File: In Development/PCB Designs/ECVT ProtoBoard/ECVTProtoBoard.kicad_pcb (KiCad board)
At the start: 2 copper layers, 26 parts, among them J1 Motor Driver, J10 3V3, J11 GND, J12 Hall Effect, J13 Hall Effect 2, J14 12V In, J15 Conn_01x08, J16 MotorDriver2, J17 GND In, J2 Conn_01x01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

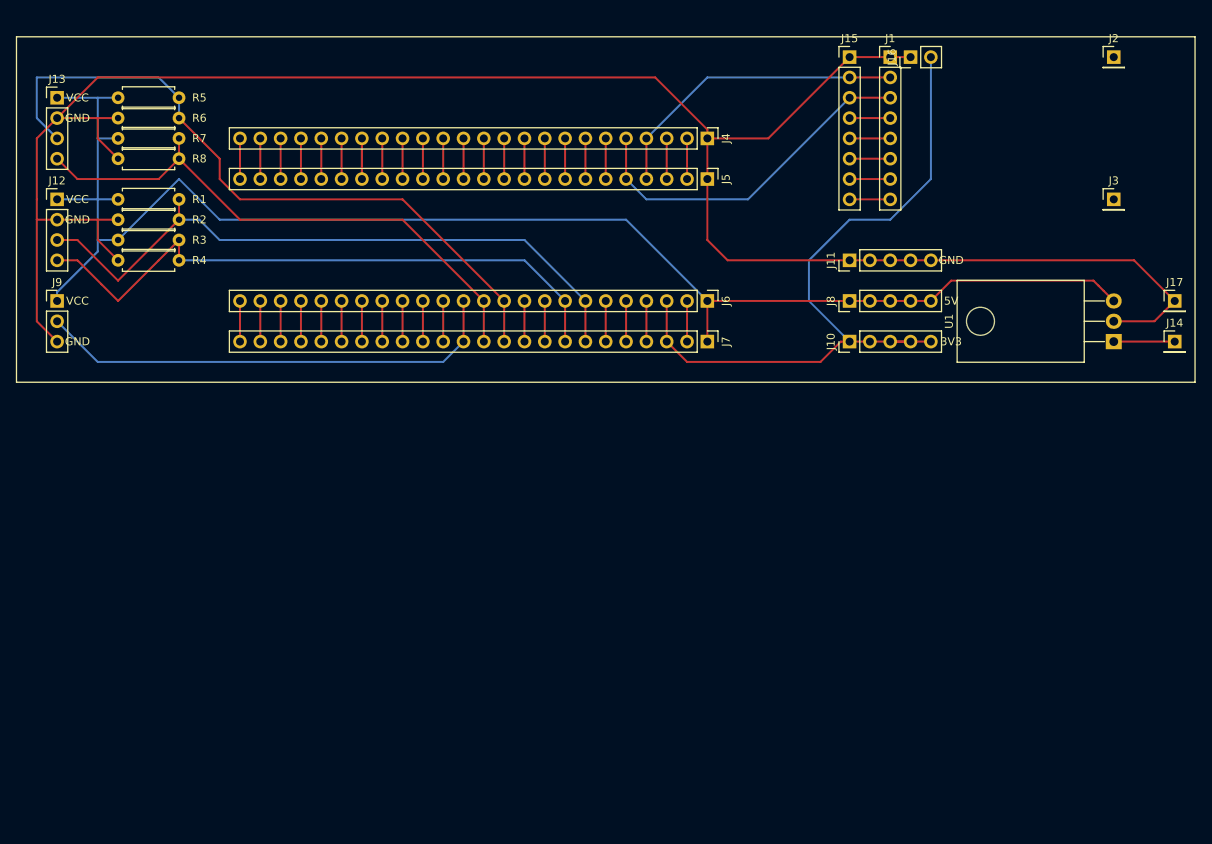
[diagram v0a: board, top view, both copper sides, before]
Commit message: Finished eCVT protoboard schematic
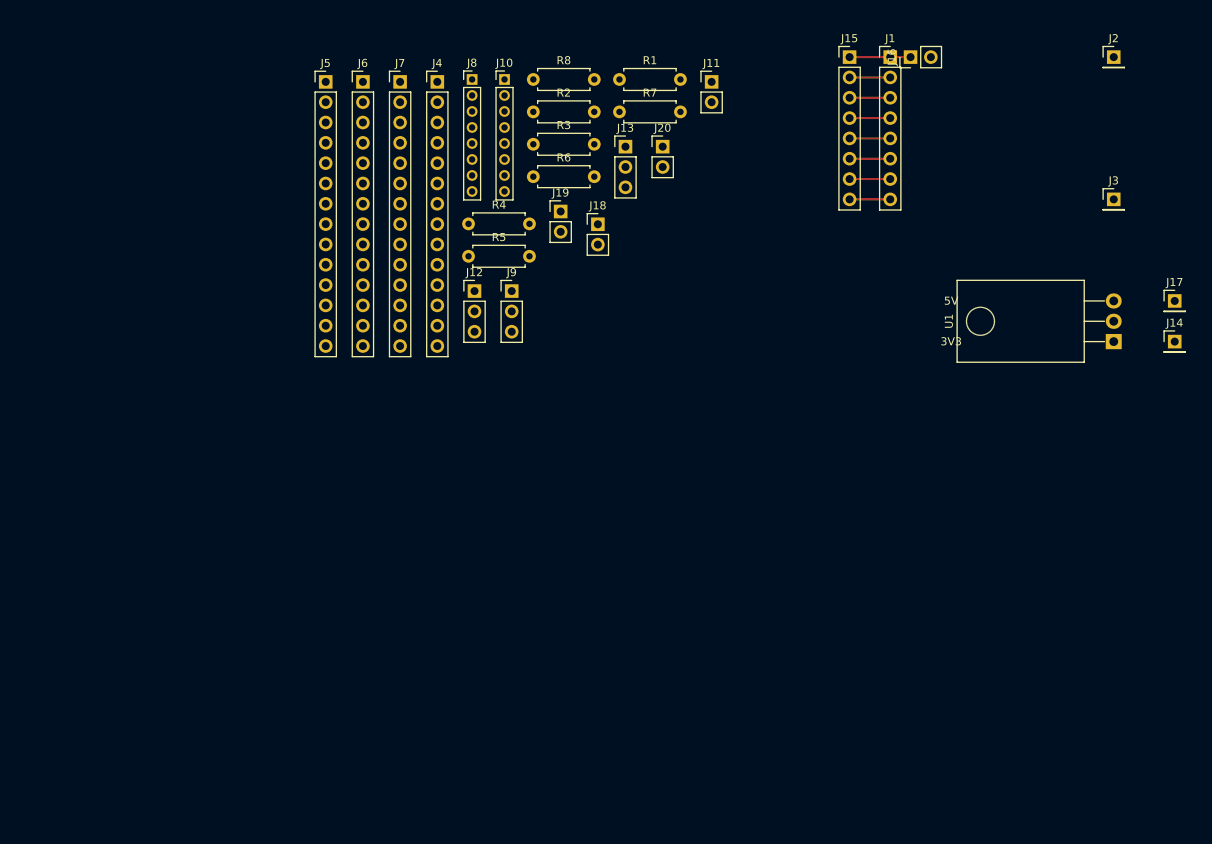
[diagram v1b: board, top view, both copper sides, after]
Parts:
- added J18: 3V3, Connector_PinHeader_2.54mm:PinHeader_1x02_P2.54mm_Vertical, F.Cu at (133.6, 92.0)
- added J19: GND, Connector_PinHeader_2.54mm:PinHeader_1x02_P2.54mm_Vertical, F.Cu at (129.0, 90.4)
- added J20: BrakeIn, Connector_PinHeader_2.54mm:PinHeader_1x02_P2.54mm_Vertical, F.Cu at (141.7, 82.3)
- J10: value 3V3 -> Conn_01x08; footprint Connector_PinHeader_2.54mm:PinHeader_1x05_P2.54mm_Vertical -> Connector_PinHeader_2.00mm:PinHeader_1x08_P2.00mm_Vertical
- J11: value GND -> 5V; footprint Connector_PinHeader_2.54mm:PinHeader_1x05_P2.54mm_Vertical -> Connector_PinHeader_2.54mm:PinHeader_1x02_P2.54mm_Vertical
- J12: footprint Connector_PinHeader_2.54mm:PinHeader_1x04_P2.54mm_Vertical -> Connector_PinHeader_2.54mm:PinHeader_1x03_P2.54mm_Vertical
- J13: value Hall Effect 2 -> Hall Effect; footprint Connector_PinHeader_2.54mm:PinHeader_1x04_P2.54mm_Vertical -> Connector_PinHeader_2.54mm:PinHeader_1x03_P2.54mm_Vertical
- J4, J7: value 1x24 -> 1x14; footprint Connector_PinHeader_2.54mm:PinHeader_1x24_P2.54mm_Vertical -> Connector_PinHeader_2.54mm:PinHeader_1x14_P2.54mm_Vertical
- J5: value Teensy 3.6L -> Teensy 3.2L; footprint Connector_PinHeader_2.54mm:PinHeader_1x24_P2.54mm_Vertical -> Connector_PinHeader_2.54mm:PinHeader_1x14_P2.54mm_Vertical
- J6: value Teensy 3.6R -> Teensy 3.2R; footprint Connector_PinHeader_2.54mm:PinHeader_1x24_P2.54mm_Vertical -> Connector_PinHeader_2.54mm:PinHeader_1x14_P2.54mm_Vertical
- J8: value 5V -> Conn_01x08; footprint Connector_PinHeader_2.54mm:PinHeader_1x05_P2.54mm_Vertical -> Connector_PinHeader_2.00mm:PinHeader_1x08_P2.00mm_Vertical
- R3, R7: value 5.1k -> 4.7k
- moved J13 71.3 mm to (137.1, 82.3)
- moved R1 57.1 mm to (136.3, 73.9), turned to 0 degrees
- moved J9 56.8 mm to (122.9, 100.4)
- moved R7 55.2 mm to (136.3, 78.0), turned to 0 degrees
- moved J8 54.7 mm to (117.9, 73.9), turned to 0 degrees
- moved J10 54.2 mm to (122.0, 73.9), turned to 0 degrees
- moved J12 53.4 mm to (118.2, 100.4)
- moved J6 51.0 mm to (104.3, 74.2), turned to 0 degrees
- moved J7 50.3 mm to (108.9, 74.2), turned to 0 degrees
- moved J5 49.2 mm to (99.6, 74.2), turned to 0 degrees
- moved R2 46.3 mm to (125.6, 78.0), turned to 0 degrees
- moved R3 45.9 mm to (125.6, 82.0), turned to 0 degrees
- moved R8 45.4 mm to (125.6, 73.9), turned to 0 degrees
- moved R6 44.9 mm to (125.6, 86.1), turned to 0 degrees
- moved R5 41.3 mm to (117.5, 96.0), turned to 0 degrees
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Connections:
- J10 pad 2: Net-(J10-Pad1) -> (no net)
- J10 pad 3: Net-(J10-Pad1) -> Net-(J1-Pad1)
- J10 pad 4: Net-(J10-Pad1) -> Net-(J10-Pad4)
- J10 pad 5: Net-(J10-Pad1) -> (no net)
- J11 pad 1: Net-(J1-Pad1) -> Net-(J10-Pad1)
- J11 pad 2: Net-(J1-Pad1) -> Net-(J10-Pad1)
- J12 pad 1: Net-(J12-Pad1) -> Net-(J10-Pad1)
- J12 pad 3: Net-(J12-Pad3) -> Net-(J10-Pad8)
- J13 pad 1: Net-(J12-Pad1) -> Net-(J10-Pad1)
- J13 pad 3: Net-(J13-Pad3) -> Net-(J10-Pad4)
- J16 pad 2: Net-(J10-Pad1) -> Net-(J16-Pad2)
- J4 pad 7: Net-(J4-Pad7) -> Net-(J10-Pad8)
- J4 pad 8: Net-(J4-Pad8) -> Net-(J10-Pad4)
- J5 pad 7: Net-(J4-Pad7) -> Net-(J10-Pad8)
- J5 pad 8: Net-(J4-Pad8) -> Net-(J10-Pad4)
- J6 pad 1: Net-(J12-Pad1) -> Net-(J10-Pad1)
- J6 pad 11: Net-(J13-Pad3) -> Net-(J6-Pad11)
- J6 pad 12: Net-(J13-Pad4) -> Net-(J6-Pad12)
- J6 pad 3: Net-(J10-Pad1) -> Net-(J16-Pad2)
- J6 pad 7: Net-(J12-Pad3) -> Net-(J6-Pad7)
- J6 pad 8: Net-(J12-Pad4) -> Net-(J6-Pad8)
- J7 pad 1: Net-(J12-Pad1) -> Net-(J10-Pad1)
- J7 pad 11: Net-(J13-Pad3) -> Net-(J6-Pad11)
- J7 pad 12: Net-(J13-Pad4) -> Net-(J6-Pad12)
- J7 pad 3: Net-(J10-Pad1) -> Net-(J16-Pad2)
- J7 pad 7: Net-(J12-Pad3) -> Net-(J6-Pad7)
- J7 pad 8: Net-(J12-Pad4) -> Net-(J6-Pad8)
- J8 pad 1: Net-(J12-Pad1) -> (no net)
- J8 pad 2: Net-(J12-Pad1) -> (no net)
- J8 pad 3: Net-(J12-Pad1) -> (no net)
- J8 pad 4: Net-(J12-Pad1) -> (no net)
- J8 pad 5: Net-(J12-Pad1) -> (no net)
- J9 pad 1: Net-(J12-Pad1) -> Net-(J16-Pad2)
- R1 pad 1: Net-(J12-Pad3) -> Net-(J10-Pad8)
- R1 pad 2: Net-(J12-Pad1) -> Net-(J10-Pad1)
- R2 pad 1: Net-(J12-Pad3) -> Net-(J10-Pad8)
- R3 pad 1: Net-(J12-Pad4) -> Net-(J6-Pad12)
- R3 pad 2: Net-(J12-Pad1) -> Net-(J20-Pad1)
- R4 pad 1: Net-(J12-Pad4) -> Net-(J1-Pad1)
- R4 pad 2: Net-(J1-Pad1) -> Net-(J6-Pad12)
- R5 pad 1: Net-(J13-Pad3) -> Net-(J10-Pad4)
- R5 pad 2: Net-(J12-Pad1) -> Net-(J10-Pad1)
- R6 pad 1: Net-(J13-Pad3) -> Net-(J10-Pad4)
- R7 pad 1: Net-(J13-Pad4) -> Net-(J6-Pad11)
- R7 pad 2: Net-(J12-Pad1) -> Net-(J20-Pad2)
- R8 pad 1: Net-(J13-Pad4) -> Net-(J1-Pad1)
- R8 pad 2: Net-(J1-Pad1) -> Net-(J6-Pad11)
- U1 pad 3: Net-(J12-Pad1) -> Net-(J10-Pad1)
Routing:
- net Net-(J1-Pad1): track 259.8 -> 7.62 mm
- net Net-(J12-Pad1): track 188.9 -> 0.00 mm
- net Net-(J10-Pad1): track 89.7 -> 0.00 mm
- net Net-(J13-Pad3): track 86.7 -> 0.00 mm
- net Net-(J12-Pad3): track 83.1 -> 0.00 mm
- net Net-(J12-Pad4): track 78.5 -> 0.00 mm
- net Net-(J13-Pad4): track 70.4 -> 0.00 mm
- net Net-(J6-Pad13): track 59.0 -> 0.00 mm
- net Net-(J1-Pad3): track 44.4 -> 5.08 mm
- net Net-(J1-Pad2): track 38.7 -> 5.08 mm
- net Net-(J4-Pad18): track 9.36 -> 0.00 mm
- net Net-(J14-Pad1): track 7.62 -> 0.00 mm
- net Net-(J6-Pad9): track 5.08 -> 0.00 mm
- net Net-(J6-Pad6): track 5.08 -> 0.00 mm
- net Net-(J6-Pad5): track 5.08 -> 0.00 mm
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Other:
- board text removed: "GND"
- board text removed: "VCC"

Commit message: Routed the board
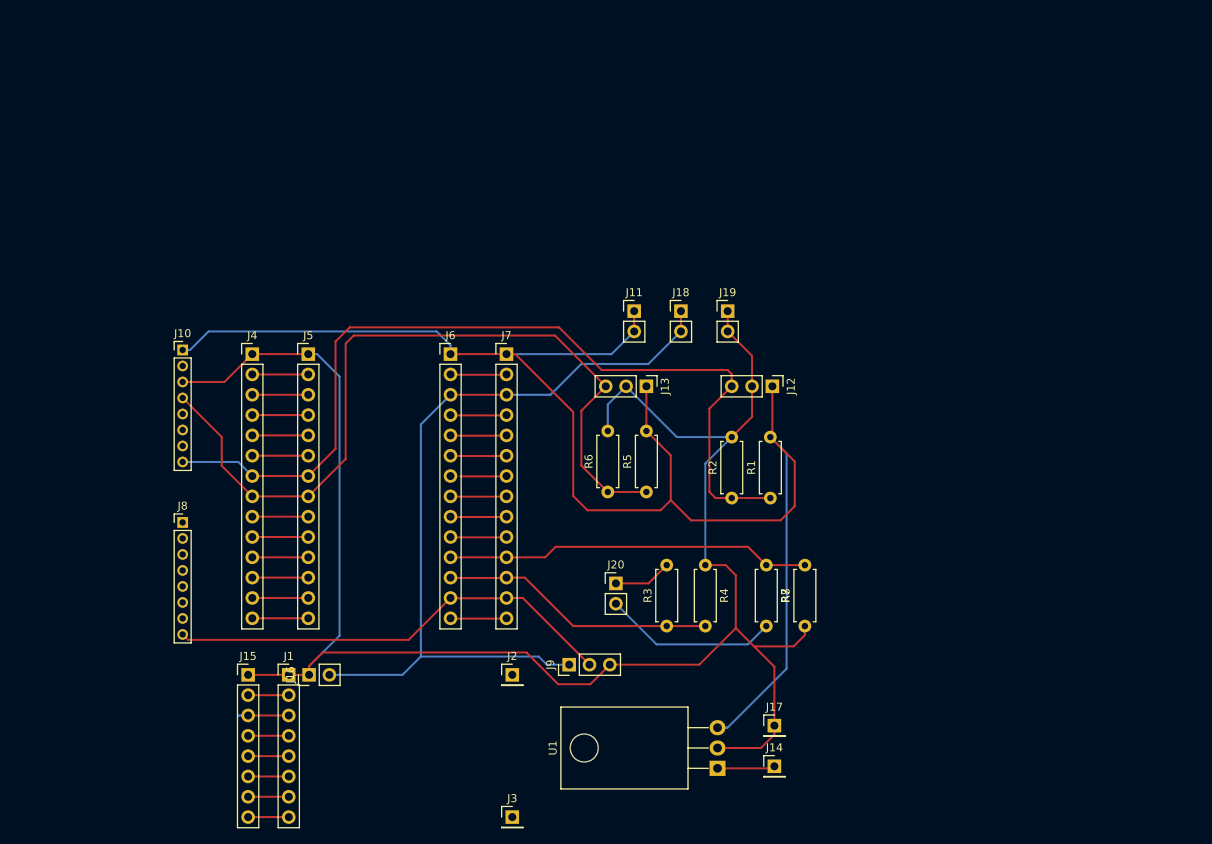
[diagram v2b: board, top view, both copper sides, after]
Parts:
- moved J1 107.8 mm to (95.0, 148.3)
- moved J15 107.8 mm to (89.9, 148.3)
- moved J16 107.8 mm to (97.5, 148.3)
- moved J2 107.8 mm to (122.9, 148.3)
- moved J3 107.8 mm to (122.9, 166.1)
- moved R8 76.3 mm to (159.5, 142.2), turned to 90 degrees
- moved J17 73.0 mm to (155.7, 154.7)
- moved J14 73.0 mm to (155.7, 159.8)
- moved U1 72.8 mm to (148.6, 160.0)
- moved J8 66.1 mm to (81.7, 129.3)
- moved R3 62.5 mm to (142.2, 142.2), turned to 90 degrees
- moved R7 59.6 mm to (154.7, 134.6), turned to 270 degrees
- moved R1 55.6 mm to (155.2, 126.2), turned to 90 degrees
- moved J20 54.9 mm to (135.9, 136.9)
- moved R2 54.3 mm to (150.4, 126.2), turned to 90 degrees
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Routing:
- net Net-(J1-Pad1): track 7.62 -> 228.3 mm
- net Net-(J10-Pad1): track 0.00 -> 188.8 mm
- net Net-(J10-Pad8): track 0.00 -> 111.2 mm
- net Net-(J16-Pad2): track 0.00 -> 100.2 mm
- net Net-(J10-Pad4): track 0.00 -> 100.2 mm
- net Net-(J6-Pad13): track 0.00 -> 56.8 mm
- net Net-(J6-Pad11): track 0.00 -> 45.8 mm
- net Net-(J6-Pad12): track 0.00 -> 34.4 mm
- net Net-(J20-Pad2): track 0.00 -> 21.8 mm
- net Net-(J1-Pad3): track 5.08 -> 13.4 mm
- net Net-(J20-Pad1): track 0.00 -> 7.30 mm
- net Net-(J14-Pad1): track 0.00 -> 7.22 mm
- net Net-(J6-Pad9): track 0.00 -> 7.00 mm
- net Net-(J6-Pad8): track 0.00 -> 7.00 mm
- net Net-(J6-Pad6): track 0.00 -> 7.00 mm
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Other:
- board text removed: "3V3"
- board text removed: "5V"

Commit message: Finished eCVT PCB rev 2
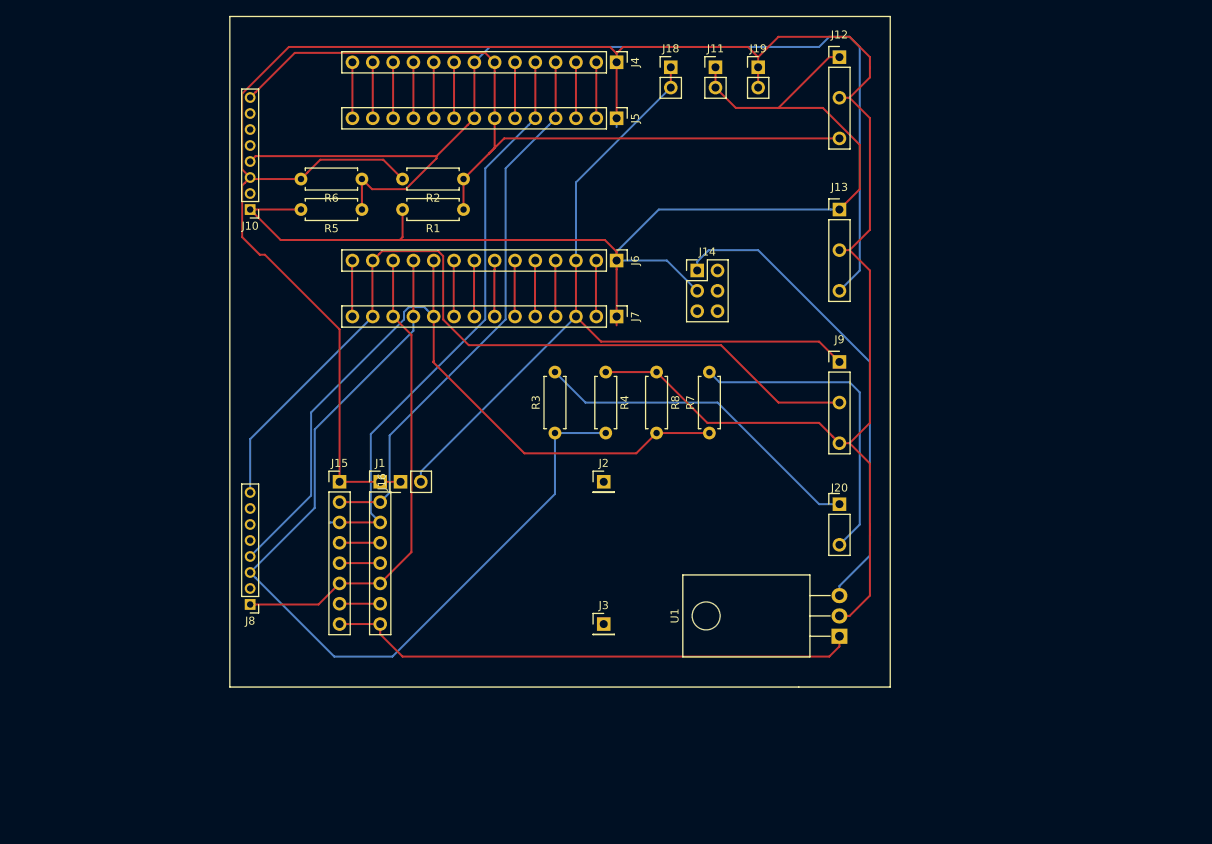
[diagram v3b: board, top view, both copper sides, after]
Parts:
- removed J17: GND In, Connector_PinHeader_2.54mm:PinHeader_1x01_P2.54mm_Vertical
- J12, J13, J9: footprint Connector_PinHeader_2.54mm:PinHeader_1x03_P2.54mm_Vertical -> CustomKiCADLibrary:PinHeader_1x03_P5.08mm_Vertical
- J14: value 12V In -> External Power Switch; footprint Connector_PinHeader_2.54mm:PinHeader_1x01_P2.54mm_Vertical -> Connector_PinHeader_2.54mm:PinHeader_2x03_P2.54mm_Vertical
- J20: footprint Connector_PinHeader_2.54mm:PinHeader_1x02_P2.54mm_Vertical -> CustomKiCADLibrary:PinHeader_1x02_P5.08mm_Vertical
- moved J14 62.7 mm to (146.1, 97.8)
- moved J4 58.3 mm to (136.0, 71.8), turned to 270 degrees
- moved R1 52.6 mm to (116.8, 90.2), turned to 180 degrees
- moved R2 52.1 mm to (116.8, 86.4), turned to 180 degrees
- moved J9 50.7 mm to (163.8, 109.2), turned to 0 degrees
- moved R5 50.1 mm to (104.1, 90.2), turned to 180 degrees
- moved R6 49.7 mm to (104.1, 86.4), turned to 180 degrees
- moved J5 48.5 mm to (136.0, 78.8), turned to 270 degrees
- moved J12 42.0 mm to (163.8, 71.1), turned to 0 degrees
- moved R8 36.8 mm to (141.0, 110.5), turned to 270 degrees
- moved J13 32.7 mm to (163.8, 90.2), turned to 0 degrees
- moved J11 32.1 mm to (148.3, 72.4)
- moved J19 30.7 mm to (153.7, 72.4)
- moved J20 30.6 mm to (163.8, 124.5)
- moved J18 30.5 mm to (142.7, 72.4)
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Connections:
- J6 pad 12: Net-(J6-Pad12) -> Net-(J1-Pad6)
- J7 pad 12: Net-(J6-Pad12) -> Net-(J1-Pad6)
- J8 pad 1: (no net) -> Net-(J1-Pad6)
- J8 pad 3: (no net) -> Net-(J6-Pad11)
- J8 pad 4: (no net) -> Net-(J6-Pad10)
- R3 pad 1: Net-(J6-Pad12) -> Net-(J6-Pad11)
- R4 pad 2: Net-(J6-Pad12) -> Net-(J6-Pad11)
- R7 pad 1: Net-(J6-Pad11) -> Net-(J6-Pad10)
- R8 pad 2: Net-(J6-Pad11) -> Net-(J6-Pad10)
- U1 pad 1: Net-(J14-Pad1) -> Net-(J1-Pad8)
- U1 pad 3: Net-(J10-Pad1) -> Net-(J14-Pad1)
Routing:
- net Net-(J6-Pad10): track 7.00 -> 96.0 mm
- net Net-(J1-Pad1): track 228.3 -> 297.2 mm
- net Net-(J6-Pad11): track 45.8 -> 112.3 mm
- net Net-(J1-Pad8): track 5.08 -> 66.7 mm
- net Net-(J1-Pad3): track 13.4 -> 72.9 mm
- net Net-(J1-Pad2): track 12.1 -> 69.1 mm
- net Net-(J1-Pad6): track 5.08 -> 60.3 mm
- net Net-(J14-Pad1): track 7.22 -> 59.9 mm
- net Net-(J6-Pad13): track 56.8 -> 106.7 mm
- net Net-(J10-Pad1): track 188.8 -> 153.2 mm
- net Net-(J20-Pad1): track 7.30 -> 42.4 mm
- net Net-(J6-Pad12): track 34.4 -> 0.00 mm
- net Net-(J10-Pad4): track 100.2 -> 134.4 mm
- net Net-(J20-Pad2): track 21.8 -> 40.0 mm
- net Net-(J10-Pad8): track 111.2 -> 98.0 mm
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
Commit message: Finished DAQ board and ready for initial production
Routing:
- net Net-(J1-Pad6): track 60.3 -> 48.0 mm
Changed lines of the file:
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@@
     (thickness 1.6)
     (drawings 7)
-    (tracks 228)
+    (tracks 226)
     (zones 0)
     (modules 28)
@@
   (segment (start 114.3 103.929004) (end 114.3 95.991) (width 0.25) (layer F.Cu) (net 19))
   (segment (start 101.346 136.906) (end 106.426 136.906) (width 0.25) (layer F.Cu) (net 20) (status 30))
-  (segment (start 98.712 139.54) (end 101.346 136.906) (width 0.25) (layer F.Cu) (net 20) (status 20))
-  (segment (start 90.17 139.54) (end 98.712 139.54) (width 0.25) (layer F.Cu) (net 20) (status 10))
   (segment (start 108.885998 104.396) (end 108.035999 103.546001) (width 0.25) (layer F.Cu) (net 20) (status 20))
   (segment (start 110.330999 105.841001) (end 108.885998 104.396) (width 0.25) (layer F.Cu) (net 20))
